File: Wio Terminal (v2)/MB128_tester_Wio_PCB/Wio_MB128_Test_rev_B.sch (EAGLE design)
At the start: 18 parts, among them IC1 SN74LVC2T45DCTR, IC2 SN74LVC2T45DCTR, IC3 SN74LVC2T45DCTR, J1 Joypad, J2 MD-80SGK, J3 CONN_20X2

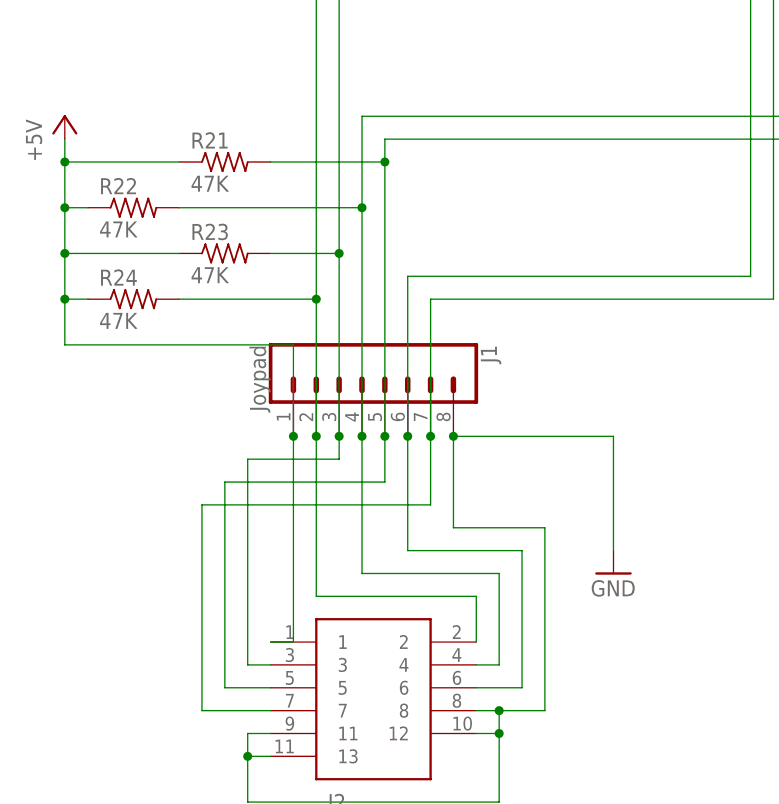
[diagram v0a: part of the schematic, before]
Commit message: Update board revision for Wio Terminal
- Update board revision for Wio Terminal, including the files required for JLCPCB to perform SMD assembly of the board.
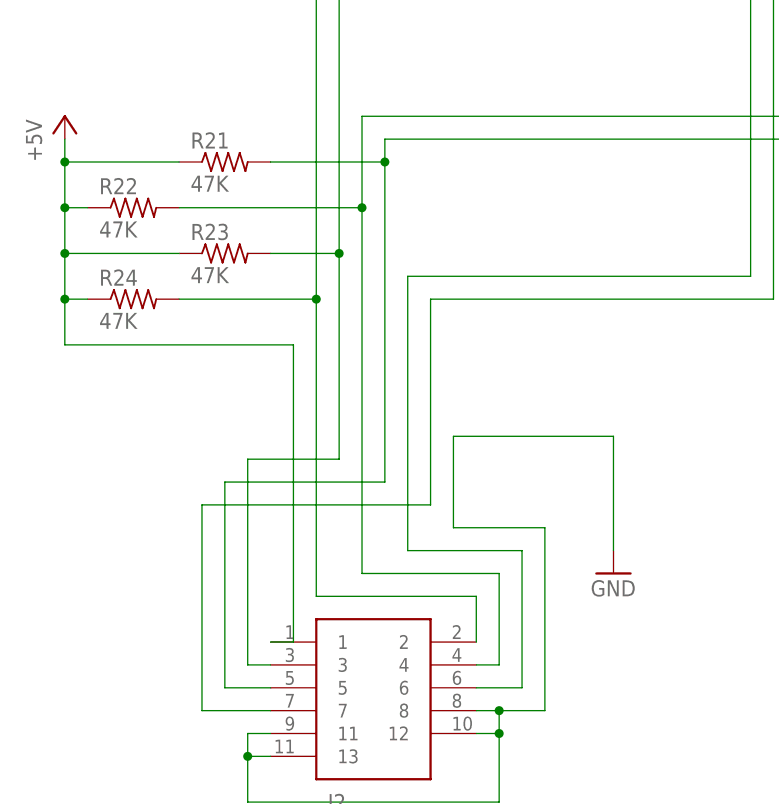
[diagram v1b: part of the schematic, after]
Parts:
- removed J1: Joypad, SparkFun-Connectors:CONN_08"
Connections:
- net +5V: no longer J1.1
- net CLR: no longer J1.7
- net GND: no longer J1.8
- net N$16: no longer J1.4
- net N$18: no longer J1.5
- net N$2: no longer J1.3
- net N$3: no longer J1.2
- net SEL: no longer J1.6
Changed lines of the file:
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@@
 <part name="J2" library="SamacSys_Parts" deviceset="MD-80SGK" device=""/>
 <part name="IC2" library="SamacSys_Parts" deviceset="SN74LVC2T45DCTR" device=""/>
-<part name="J1" library="SparkFun-Connectors" library_urn="urn:adsk.eagle:library:513" deviceset="CONN_08" device="&quot;" package3d_urn="urn:adsk.eagle:package:38138/1" value="Joypad"/>
 <part name="GND1" library="supply1" deviceset="GND" device=""/>
 <part name="GND2" library="supply1" deviceset="GND" device=""/>
@@
 <attribute name="VALUE" x="125.73" y="180.34" size="1.778" layer="96" align="center-left"/>
 </instance>
-<instance part="J1" gate="G$1" x="50.8" y="50.8" smashed="yes" rot="R270">
-<attribute name="VALUE" x="38.354" y="55.88" size="1.778" layer="96" font="vector" rot="R270"/>
-<attribute name="NAME" x="64.008" y="55.88" size="1.778" layer="95" font="vector" rot="R270"/>
-</instance>
 <instance part="GND1" gate="1" x="154.94" y="177.8" smashed="yes">
 <attribute name="VALUE" x="152.4" y="175.26" size="1.778" layer="96"/>
@@
 <net name="N$3" class="2">
 <segment>
-<pinref part="J1" gate="G$1" pin="2"/>
-<wire x1="45.72" y1="45.72" x2="45.72" y2="27.94" width="0.1524" layer="91"/>
+<wire x1="45.72" y1="60.96" x2="45.72" y2="27.94" width="0.1524" layer="91"/>
 <pinref part="J2" gate="G$1" pin="2"/>
 <wire x1="45.72" y1="27.94" x2="63.5" y2="27.94" width="0.1524" layer="91"/>
 <wire x1="63.5" y1="27.94" x2="63.5" y2="22.86" width="0.1524" layer="91"/>
-<junction x="45.72" y="45.72"/>
-<wire x1="45.72" y1="45.72" x2="45.72" y2="60.96" width="0.1524" layer="91"/>
 <pinref part="R24" gate="G$1" pin="2"/>
 <wire x1="30.48" y1="60.96" x2="45.72" y2="60.96" width="0.1524" layer="91"/>
@@
 <net name="SEL" class="2">
 <segment>
-<pinref part="J1" gate="G$1" pin="6"/>
-<wire x1="55.88" y1="45.72" x2="55.88" y2="33.02" width="0.1524" layer="91"/>
 <wire x1="55.88" y1="33.02" x2="68.58" y2="33.02" width="0.1524" layer="91"/>
 <pinref part="J2" gate="G$1" pin="6"/>
@@
 <wire x1="68.58" y1="17.78" x2="63.5" y2="17.78" width="0.1524" layer="91"/>
 <wire x1="93.98" y1="63.5" x2="55.88" y2="63.5" width="0.1524" layer="91"/>
-<wire x1="55.88" y1="63.5" x2="55.88" y2="45.72" width="0.1524" layer="91"/>
-<junction x="55.88" y="45.72"/>
+<wire x1="55.88" y1="63.5" x2="55.88" y2="33.02" width="0.1524" layer="91"/>
 <wire x1="93.98" y1="139.7" x2="93.98" y2="63.5" width="0.1524" layer="91"/>
 <pinref part="R16" gate="G$1" pin="1"/>
@@
 <net name="CLR" class="2">
 <segment>
-<pinref part="J1" gate="G$1" pin="7"/>
-<wire x1="58.42" y1="45.72" x2="58.42" y2="38.1" width="0.1524" layer="91"/>
 <wire x1="58.42" y1="38.1" x2="33.02" y2="38.1" width="0.1524" layer="91"/>
 <pinref part="J2" gate="G$1" pin="7"/>
@@
 <wire x1="33.02" y1="15.24" x2="40.64" y2="15.24" width="0.1524" layer="91"/>
 <wire x1="96.52" y1="60.96" x2="58.42" y2="60.96" width="0.1524" layer="91"/>
-<wire x1="58.42" y1="60.96" x2="58.42" y2="45.72" width="0.1524" layer="91"/>
-<junction x="58.42" y="45.72"/>
+<wire x1="58.42" y1="60.96" x2="58.42" y2="38.1" width="0.1524" layer="91"/>
 <wire x1="96.52" y1="147.32" x2="96.52" y2="60.96" width="0.1524" layer="91"/>
 <pinref part="R18" gate="G$1" pin="1"/>
@@
 </segment>
 <segment>
-<pinref part="J1" gate="G$1" pin="8"/>
 <wire x1="60.96" y1="45.72" x2="60.96" y2="35.56" width="0.1524" layer="91"/>
 <wire x1="60.96" y1="35.56" x2="71.12" y2="35.56" width="0.1524" layer="91"/>
@@
 <wire x1="66.04" y1="15.24" x2="63.5" y2="15.24" width="0.1524" layer="91"/>
 <wire x1="60.96" y1="45.72" x2="78.74" y2="45.72" width="0.1524" layer="91"/>
-<junction x="60.96" y="45.72"/>
 <pinref part="GND9" gate="1" pin="GND"/>
 <wire x1="78.74" y1="45.72" x2="78.74" y2="33.02" width="0.1524" layer="91"/>
@@
 <segment>
 <pinref part="J2" gate="G$1" pin="3"/>
-<pinref part="J1" gate="G$1" pin="3"/>
-<junction x="48.26" y="45.72"/>
-<wire x1="48.26" y1="45.72" x2="48.26" y2="43.18" width="0.1524" layer="91"/>
 <wire x1="48.26" y1="43.18" x2="38.1" y2="43.18" width="0.1524" layer="91"/>
 <wire x1="38.1" y1="43.18" x2="38.1" y2="20.32" width="0.1524" layer="91"/>
 <wire x1="38.1" y1="20.32" x2="40.64" y2="20.32" width="0.1524" layer="91"/>
-<wire x1="48.26" y1="45.72" x2="48.26" y2="66.04" width="0.1524" layer="91"/>
+<wire x1="48.26" y1="43.18" x2="48.26" y2="66.04" width="0.1524" layer="91"/>
 <wire x1="40.64" y1="66.04" x2="48.26" y2="66.04" width="0.1524" layer="91"/>
 <pinref part="R23" gate="G$1" pin="2"/>
@@
 <segment>
 <pinref part="J2" gate="G$1" pin="1"/>
-<pinref part="J1" gate="G$1" pin="1"/>
 <wire x1="40.64" y1="22.86" x2="43.18" y2="22.86" width="0.1524" layer="91"/>
-<wire x1="43.18" y1="22.86" x2="43.18" y2="45.72" width="0.1524" layer="91"/>
-<wire x1="43.18" y1="55.88" x2="43.18" y2="45.72" width="0.1524" layer="91"/>
-<junction x="43.18" y="45.72"/>
+<wire x1="43.18" y1="22.86" x2="43.18" y2="55.88" width="0.1524" layer="91"/>
 <wire x1="43.18" y1="55.88" x2="17.78" y2="55.88" width="0.1524" layer="91"/>
 <wire x1="17.78" y1="55.88" x2="17.78" y2="60.96" width="0.1524" layer="91"/>
@@
 <net name="N$16" class="0">
 <segment>
-<pinref part="J1" gate="G$1" pin="4"/>
-<wire x1="50.8" y1="45.72" x2="50.8" y2="30.48" width="0.1524" layer="91"/>
 <wire x1="50.8" y1="30.48" x2="66.04" y2="30.48" width="0.1524" layer="91"/>
 <pinref part="J2" gate="G$1" pin="4"/>
 <wire x1="66.04" y1="30.48" x2="66.04" y2="20.32" width="0.1524" layer="91"/>
 <wire x1="66.04" y1="20.32" x2="63.5" y2="20.32" width="0.1524" layer="91"/>
-<junction x="50.8" y="45.72"/>
-<wire x1="50.8" y1="45.72" x2="50.8" y2="71.12" width="0.1524" layer="91"/>
+<wire x1="50.8" y1="30.48" x2="50.8" y2="71.12" width="0.1524" layer="91"/>
 <pinref part="R22" gate="G$1" pin="2"/>
 <wire x1="30.48" y1="71.12" x2="50.8" y2="71.12" width="0.1524" layer="91"/>
@@
 <net name="N$18" class="0">
 <segment>
-<pinref part="J1" gate="G$1" pin="5"/>
-<wire x1="53.34" y1="45.72" x2="53.34" y2="40.64" width="0.1524" layer="91"/>
 <wire x1="53.34" y1="40.64" x2="35.56" y2="40.64" width="0.1524" layer="91"/>
 <pinref part="J2" gate="G$1" pin="5"/>
 <wire x1="35.56" y1="40.64" x2="35.56" y2="17.78" width="0.1524" layer="91"/>
 <wire x1="35.56" y1="17.78" x2="40.64" y2="17.78" width="0.1524" layer="91"/>
-<junction x="53.34" y="45.72"/>
-<wire x1="53.34" y1="45.72" x2="53.34" y2="76.2" width="0.1524" layer="91"/>
+<wire x1="53.34" y1="40.64" x2="53.34" y2="76.2" width="0.1524" layer="91"/>
 <wire x1="40.64" y1="76.2" x2="53.34" y2="76.2" width="0.1524" layer="91"/>
 <pinref part="R21" gate="G$1" pin="2"/>
